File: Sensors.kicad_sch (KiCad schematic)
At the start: 8 parts, among them U01 BMI270, U02 BMM150

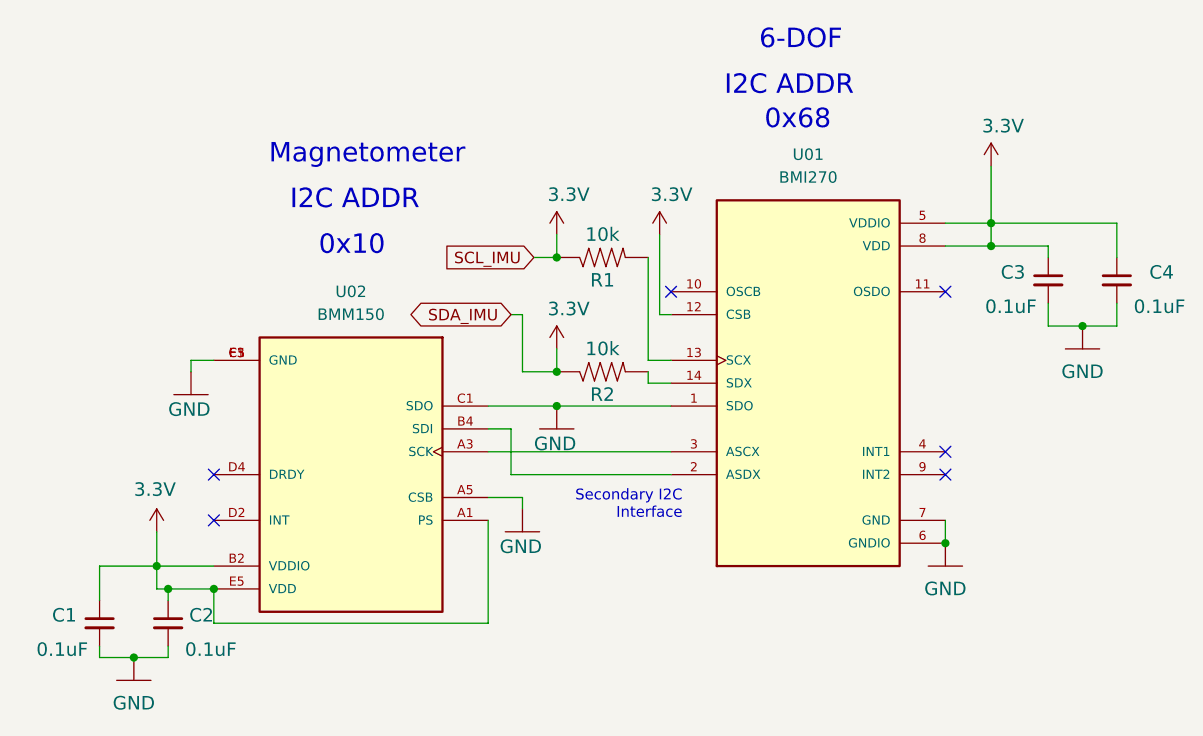
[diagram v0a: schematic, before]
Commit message: Added Pin Headers to Schematic and PCB
6 pin connector for
sda
scl
gnd
3.3v
sdi
sck
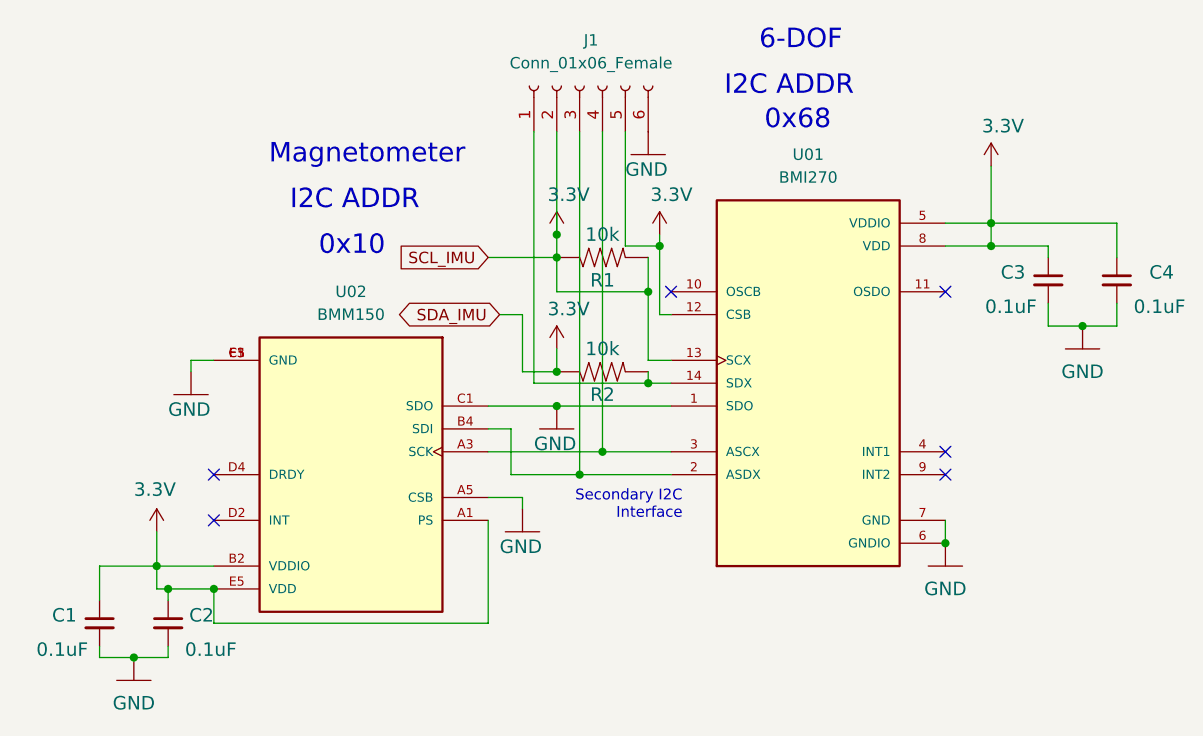
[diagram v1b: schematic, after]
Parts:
- added J1: Conn_01x06_Female, Connector_PinHeader_2.54mm:PinHeader_1x06_P2.54mm_Horizontal, symbol Connector:Conn_01x06_Female
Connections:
- net 3.3V: now also R1.2, U01.13 (SCX), J1.2 (Pin_2), J1.5 (Pin_5)
- net GND: now also J1.6 (Pin_6)
- net at U01.3 (ASCX), U02.A3 (SCK): now also J1.4 (Pin_4)
- net at U01.2 (ASDX), U02.B4 (SDI): now also J1.3 (Pin_3)
- net at R2.2, U01.14 (SDX): now also J1.1 (Pin_1)
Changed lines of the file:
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@@
   (junction (at 180.34 114.3) (diameter 0) (color 0 0 0 0)
   )
+  (junction (at 148.59 81.28) (diameter 0) (color 0 0 0 0)
+  )
   (junction (at 93.98 119.38) (diameter 0) (color 0 0 0 0)
   )
@@
   (junction (at 99.06 119.38) (diameter 0) (color 0 0 0 0)
   )
+  (junction (at 142.24 104.14) (diameter 0) (color 0 0 0 0)
+  )
   (junction (at 185.42 81.28) (diameter 0) (color 0 0 0 0)
   )
+  (junction (at 147.32 86.36) (diameter 0) (color 0 0 0 0)
+  )
   (junction (at 137.16 99.06) (diameter 0) (color 0 0 0 0)
   )
   (junction (at 195.58 90.17) (diameter 0) (color 0 0 0 0)
   )
+  (junction (at 137.16 80.01) (diameter 0) (color 0 0 0 0)
+  )
+  (junction (at 147.32 96.52) (diameter 0) (color 0 0 0 0)
+  )
   (junction (at 137.16 82.55) (diameter 0) (color 0 0 0 0)
+  )
+  (junction (at 139.7 106.68) (diameter 0) (color 0 0 0 0)
   )
   (no_connect (at 99.06 111.76))
@@
     (stroke (width 0) (type default) (color 0 0 0 0))
   )
-  (wire (pts (xy 149.86 106.68) (xy 132.08 106.68))
-    (stroke (width 0) (type default) (color 0 0 0 0))
-  )
-  (wire (pts (xy 148.59 80.01) (xy 148.59 88.9))
+  (wire (pts (xy 129.54 99.06) (xy 137.16 99.06))
+    (stroke (width 0) (type default) (color 0 0 0 0))
+  )
+  (wire (pts (xy 137.16 86.36) (xy 147.32 86.36))
     (stroke (width 0) (type default) (color 0 0 0 0))
   )
@@
     (stroke (width 0) (type default) (color 0 0 0 0))
   )
+  (wire (pts (xy 133.35 88.9) (xy 133.35 95.25))
+    (stroke (width 0) (type default) (color 0 0 0 0))
+  )
   (wire (pts (xy 199.39 90.17) (xy 199.39 87.63))
     (stroke (width 0) (type default) (color 0 0 0 0))
@@
     (stroke (width 0) (type default) (color 0 0 0 0))
   )
-  (wire (pts (xy 147.32 82.55) (xy 147.32 93.98))
+  (wire (pts (xy 147.32 82.55) (xy 147.32 86.36))
+    (stroke (width 0) (type default) (color 0 0 0 0))
+  )
+  (wire (pts (xy 148.59 81.28) (xy 148.59 88.9))
     (stroke (width 0) (type default) (color 0 0 0 0))
   )
@@
     (stroke (width 0) (type default) (color 0 0 0 0))
   )
+  (wire (pts (xy 132.08 106.68) (xy 139.7 106.68))
+    (stroke (width 0) (type default) (color 0 0 0 0))
+  )
   (wire (pts (xy 129.54 111.76) (xy 129.54 123.19))
     (stroke (width 0) (type default) (color 0 0 0 0))
@@
     (stroke (width 0) (type default) (color 0 0 0 0))
   )
-  (wire (pts (xy 129.54 104.14) (xy 149.86 104.14))
-    (stroke (width 0) (type default) (color 0 0 0 0))
-  )
-  (wire (pts (xy 133.35 95.25) (xy 133.35 88.9))
+  (wire (pts (xy 129.54 104.14) (xy 142.24 104.14))
+    (stroke (width 0) (type default) (color 0 0 0 0))
+  )
+  (wire (pts (xy 137.16 82.55) (xy 137.16 86.36))
+    (stroke (width 0) (type default) (color 0 0 0 0))
+  )
+  (wire (pts (xy 134.62 68.58) (xy 134.62 96.52))
+    (stroke (width 0) (type default) (color 0 0 0 0))
+  )
+  (wire (pts (xy 137.16 80.01) (xy 137.16 82.55))
+    (stroke (width 0) (type default) (color 0 0 0 0))
+  )
+  (wire (pts (xy 142.24 104.14) (xy 149.86 104.14))
+    (stroke (width 0) (type default) (color 0 0 0 0))
+  )
+  (wire (pts (xy 130.81 88.9) (xy 133.35 88.9))
     (stroke (width 0) (type default) (color 0 0 0 0))
   )
@@
     (stroke (width 0) (type default) (color 0 0 0 0))
   )
-  (wire (pts (xy 129.54 99.06) (xy 137.16 99.06))
-    (stroke (width 0) (type default) (color 0 0 0 0))
-  )
   (wire (pts (xy 180.34 81.28) (xy 185.42 81.28))
     (stroke (width 0) (type default) (color 0 0 0 0))
   )
+  (wire (pts (xy 147.32 86.36) (xy 147.32 93.98))
+    (stroke (width 0) (type default) (color 0 0 0 0))
+  )
   (wire (pts (xy 92.71 113.03) (xy 92.71 116.84))
     (stroke (width 0) (type default) (color 0 0 0 0))
@@
     (stroke (width 0) (type default) (color 0 0 0 0))
   )
+  (wire (pts (xy 144.78 68.58) (xy 144.78 81.28))
+    (stroke (width 0) (type default) (color 0 0 0 0))
+  )
   (wire (pts (xy 147.32 93.98) (xy 149.86 93.98))
     (stroke (width 0) (type default) (color 0 0 0 0))
@@
     (stroke (width 0) (type default) (color 0 0 0 0))
   )
-  (wire (pts (xy 134.62 82.55) (xy 137.16 82.55))
+  (wire (pts (xy 139.7 106.68) (xy 149.86 106.68))
+    (stroke (width 0) (type default) (color 0 0 0 0))
+  )
+  (wire (pts (xy 129.54 82.55) (xy 137.16 82.55))
     (stroke (width 0) (type default) (color 0 0 0 0))
   )
@@
     (stroke (width 0) (type default) (color 0 0 0 0))
   )
+  (wire (pts (xy 134.62 96.52) (xy 147.32 96.52))
+    (stroke (width 0) (type default) (color 0 0 0 0))
+  )
   (wire (pts (xy 133.35 110.49) (xy 133.35 109.22))
     (stroke (width 0) (type default) (color 0 0 0 0))
@@
     (stroke (width 0) (type default) (color 0 0 0 0))
   )
-  (wire (pts (xy 149.86 96.52) (xy 147.32 96.52))
+  (wire (pts (xy 142.24 68.58) (xy 142.24 104.14))
     (stroke (width 0) (type default) (color 0 0 0 0))
   )
@@
     (stroke (width 0) (type default) (color 0 0 0 0))
   )
-  (wire (pts (xy 132.08 88.9) (xy 133.35 88.9))
-    (stroke (width 0) (type default) (color 0 0 0 0))
-  )
-  (wire (pts (xy 137.16 80.01) (xy 137.16 82.55))
+  (wire (pts (xy 144.78 81.28) (xy 148.59 81.28))
+    (stroke (width 0) (type default) (color 0 0 0 0))
+  )
+  (wire (pts (xy 139.7 68.58) (xy 139.7 106.68))
+    (stroke (width 0) (type default) (color 0 0 0 0))
+  )
+  (wire (pts (xy 148.59 80.01) (xy 148.59 81.28))
+    (stroke (width 0) (type default) (color 0 0 0 0))
+  )
+  (wire (pts (xy 137.16 68.58) (xy 137.16 80.01))
     (stroke (width 0) (type default) (color 0 0 0 0))
   )
@@
   )
   (wire (pts (xy 185.42 81.28) (xy 191.77 81.28))
+    (stroke (width 0) (type default) (color 0 0 0 0))
+  )
+  (wire (pts (xy 147.32 96.52) (xy 149.86 96.52))
     (stroke (width 0) (type default) (color 0 0 0 0))
   )
@@
     (effects (font (size 2.159 2.159)) (justify right bottom))
   )
-  (global_label "SDA_IMU" (shape bidirectional) (at 132.08 88.9 180) (fields_autoplaced)
+  (global_label "SDA_IMU" (shape bidirectional) (at 130.81 88.9 180) (fields_autoplaced)
     (effects (font (size 1.27 1.27)) (justify right))
-    (property "Intersheet References" "${INTERSHEET_REFS}" (id 0) (at -78.74 -53.34 0)
-      (effects (font (size 1.27 1.27)) hide)
-    )
-  )
-  (global_label "SCL_IMU" (shape input) (at 134.62 82.55 180) (fields_autoplaced)
+    (property "Intersheet References" "${INTERSHEET_REFS}" (id 0) (at -80.01 -53.34 0)
+      (effects (font (size 1.27 1.27)) hide)
+    )
+  )
+  (global_label "SCL_IMU" (shape input) (at 129.54 82.55 180) (fields_autoplaced)
     (effects (font (size 1.27 1.27)) (justify right))
-    (property "Intersheet References" "${INTERSHEET_REFS}" (id 0) (at -76.2 -57.15 0)
-      (effects (font (size 1.27 1.27)) hide)
-    )
+    (property "Intersheet References" "${INTERSHEET_REFS}" (id 0) (at -81.28 -57.15 0)
+      (effects (font (size 1.27 1.27)) hide)
+    )
+  )
+  (symbol (lib_id "Connector:Conn_01x06_Female") (at 139.7 63.5 90) (unit 1)
+    (in_bom yes) (on_board yes) (fields_autoplaced)
+    (property "Reference" "J1" (id 0) (at 140.97 58.42 90))
+    (property "Value" "Conn_01x06_Female" (id 1) (at 140.97 60.96 90))
+    (property "Footprint" "Connector_PinHeader_2.54mm:PinHeader_1x06_P2.54mm_Horizontal" (id 2) (at 139.7 63.5 0)
+      (effects (font (size 1.27 1.27)) hide)
+    )
+    (property "Datasheet" "~" (id 3) (at 139.7 63.5 0)
+      (effects (font (size 1.27 1.27)) hide)
+    )
+    (pin "1")
+    (pin "2")
+    (pin "3")
+    (pin "4")
+    (pin "5")
+    (pin "6")
   )
   (symbol (lib_id "mainboard:C_Small") (at 199.39 85.09 0) (mirror y) (unit 1)
@@
     (pin "2")
   )
+  (symbol (lib_id "mainboard:GND") (at 147.32 71.12 0) (unit 1)
+    (in_bom yes) (on_board yes)
+    (property "Reference" "#GND0107" (id 0) (at 147.32 71.12 0)
+      (effects (font (size 1.27 1.27)) hide)
+    )
+    (property "Value" "GND" (id 1) (at 144.78 73.66 0)
+      (effects (font (size 1.4986 1.4986)) (justify left bottom))
+    )
+    (property "Footprint" "" (id 2) (at 147.32 71.12 0)
+      (effects (font (size 1.27 1.27)) hide)
+    )
+    (property "Datasheet" "" (id 3) (at 147.32 71.12 0)
+      (effects (font (size 1.27 1.27)) hide)
+    )
+    (pin "1")
+  )
   (symbol (lib_id "mainboard:3.3V") (at 92.71 113.03 0) (unit 1)
     (in_bom yes) (on_board yes)
@@
       (reference "#GND0106") (unit 1) (value "GND") (footprint "")
     )
+    (path "/cb7beac1-0f71-47a4-bfc8-054320c863ef"
+      (reference "#GND0107") (unit 1) (value "GND") (footprint "")
+    )
     (path "/d958ab44-7ba5-4a62-9b17-fc492f3f39ab"
       (reference "#SUPPLY0101") (unit 1) (value "3.3V") (footprint "")
@@
       (reference "C4") (unit 1) (value "0.1uF") (footprint "Capacitor_SMD:C_0603_1608Metric")
     )
+    (path "/17a3fbef-5f0f-4bf7-a824-b114cc601e1d"
+      (reference "J1") (unit 1) (value "Conn_01x06_Female") (footprint "Connector_PinHeader_2.54mm:PinHeader_1x06_P2.54mm_Horizontal")
+    )
     (path "/8c5e1cfa-43a5-41d1-9b8f-30d01262190b"
